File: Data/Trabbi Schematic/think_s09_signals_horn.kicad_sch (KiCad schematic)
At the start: 15 parts, among them J1 Power Outlet (D60), K1 Flasher Relay R3, SW1 Horn Contact (steering wheel), SW2 Turn Signal / Hazard Switch (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, SW3 Driver Door Switch (C30), SW4 Passenger Door Switch (C31), SW5 Tailgate Switch (B10)

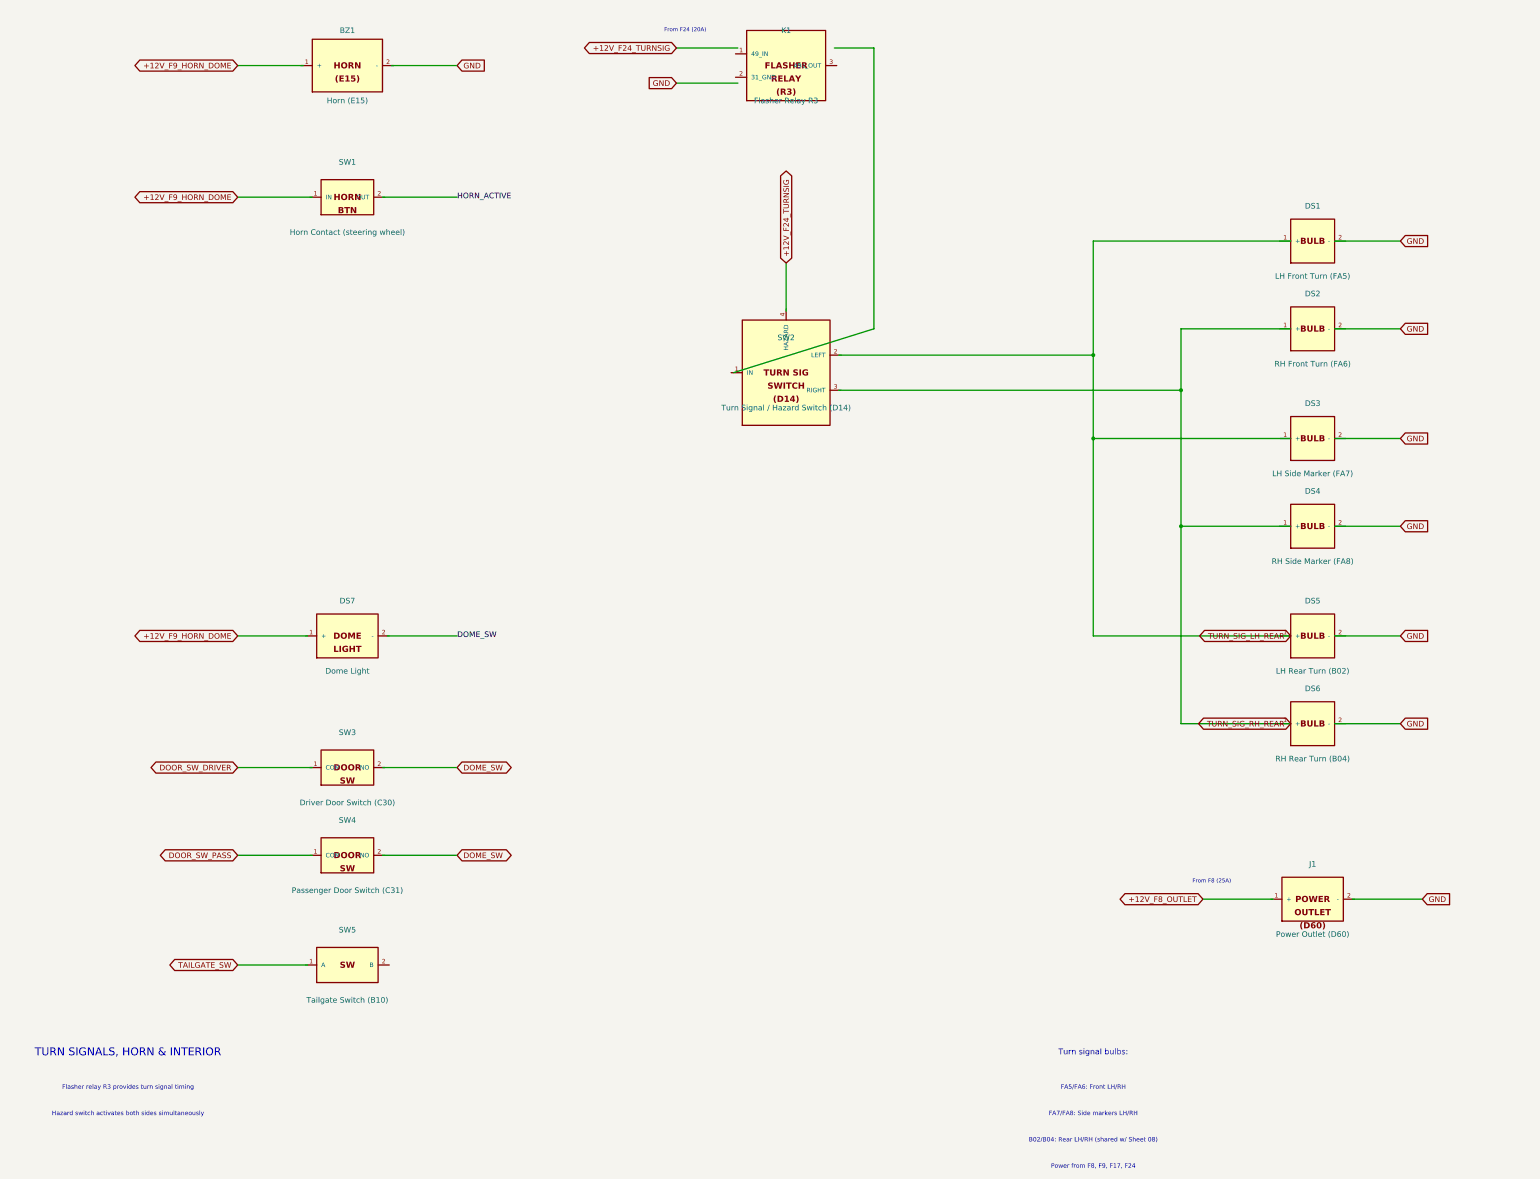
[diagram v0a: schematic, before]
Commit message: Fix wire-to-pin connections: use exact calculated pin positions
Refactored gen_think_complete.py to compute exact pin schematic
coordinates instead of using approximate manual offsets. Added p()
method to Sheet class that transforms symbol-local pin positions to
schematic coordinates. All 232 wire calls across 13 sub-sheet
generators now use p() for pin endpoints, fixing misaligned
connections (previously off by 0.54-10+ units).

Co-Authored-By: Claude Opus 4.6 <noreply@anthropic.com>
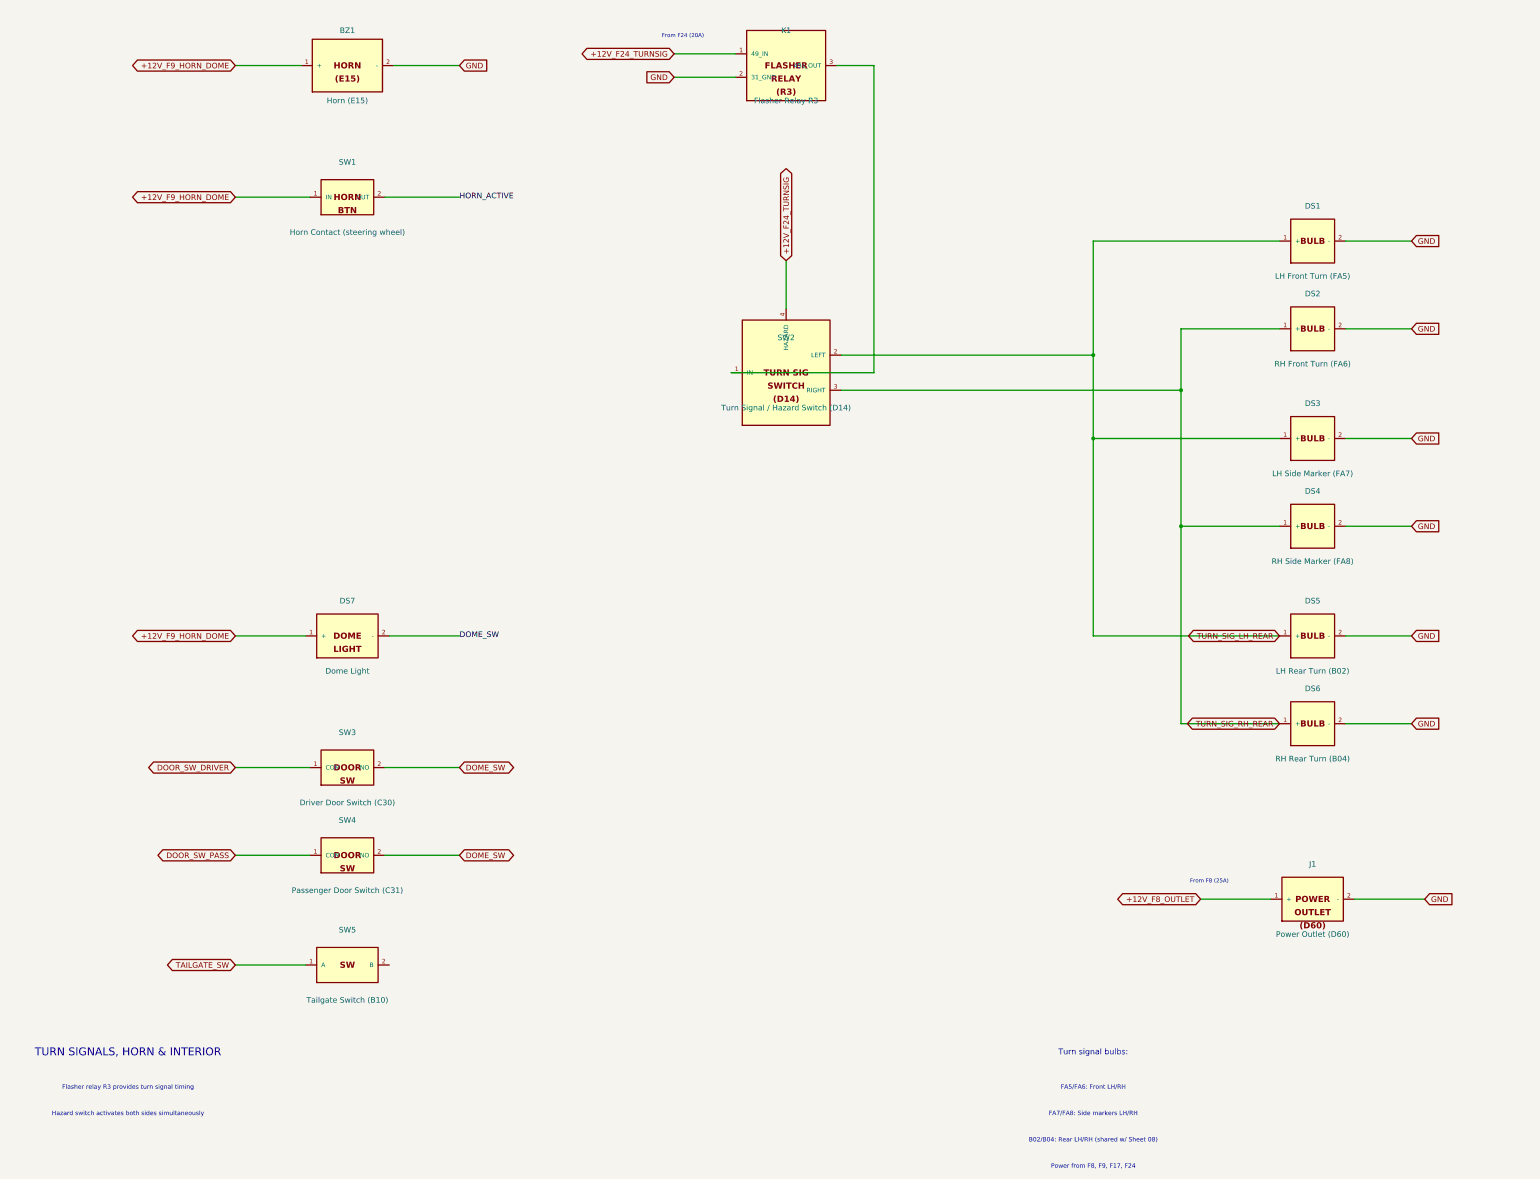
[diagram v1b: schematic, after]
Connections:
- net +12V_F24_TURNSIG: now also K1.1 (49_IN), SW2.4 (HAZARD)
- net +12V_F8_OUTLET: now also J1.1 (+)
- net +12V_F9_HORN_DOME: now also BZ1.1 (+), DS7.1 (+), SW1.1 (IN)
- net DOME_SW: now also DS7.2 (-), SW3.2 (NO), SW4.2 (NO)
- net DOOR_SW_DRIVER: now also SW3.1 (COM)
- net DOOR_SW_PASS: now also SW4.1 (COM)
- net GND: now also BZ1.2 (-), DS1.2 (-), DS2.2 (-), DS3.2 (-), DS4.2 (-), DS5.2 (-), DS6.2 (-), J1.2 (-), K1.2 (31_GND)
- net HORN_ACTIVE: now also SW1.2 (OUT)
- net TAILGATE_SW: now also SW5.1 (A)
- net TURN_SIG_LH_REAR: now also DS1.1 (+), DS3.1 (+), DS5.1 (+), SW2.2 (LEFT)
- net TURN_SIG_RH_REAR: now also DS2.1 (+), DS4.1 (+), DS6.1 (+), SW2.3 (RIGHT)
- net at SW2.1 (IN): now also K1.3 (49a_OUT)

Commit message: Enforce orthogonal routing and 1.27mm grid alignment
- Add _g() grid snap function to Sheet class (rounds all coordinates to nearest 1.27mm)
- Add wire_l() method for L-shaped orthogonal routing (horizontal+vertical segments)
- Apply grid snapping in p(), place(), wire(), label(), glabel(), junction(), no_connect(), defsym()
- Replace all 19 diagonal wire calls with wire_l() across S02, S06, S07, S08, S10, S12, S13
- All wire segments now strictly horizontal or vertical, no diagonals
- All coordinates verified on 1.27mm (50mil) KiCad standard grid

Co-Authored-By: Claude Opus 4.6 <noreply@anthropic.com>
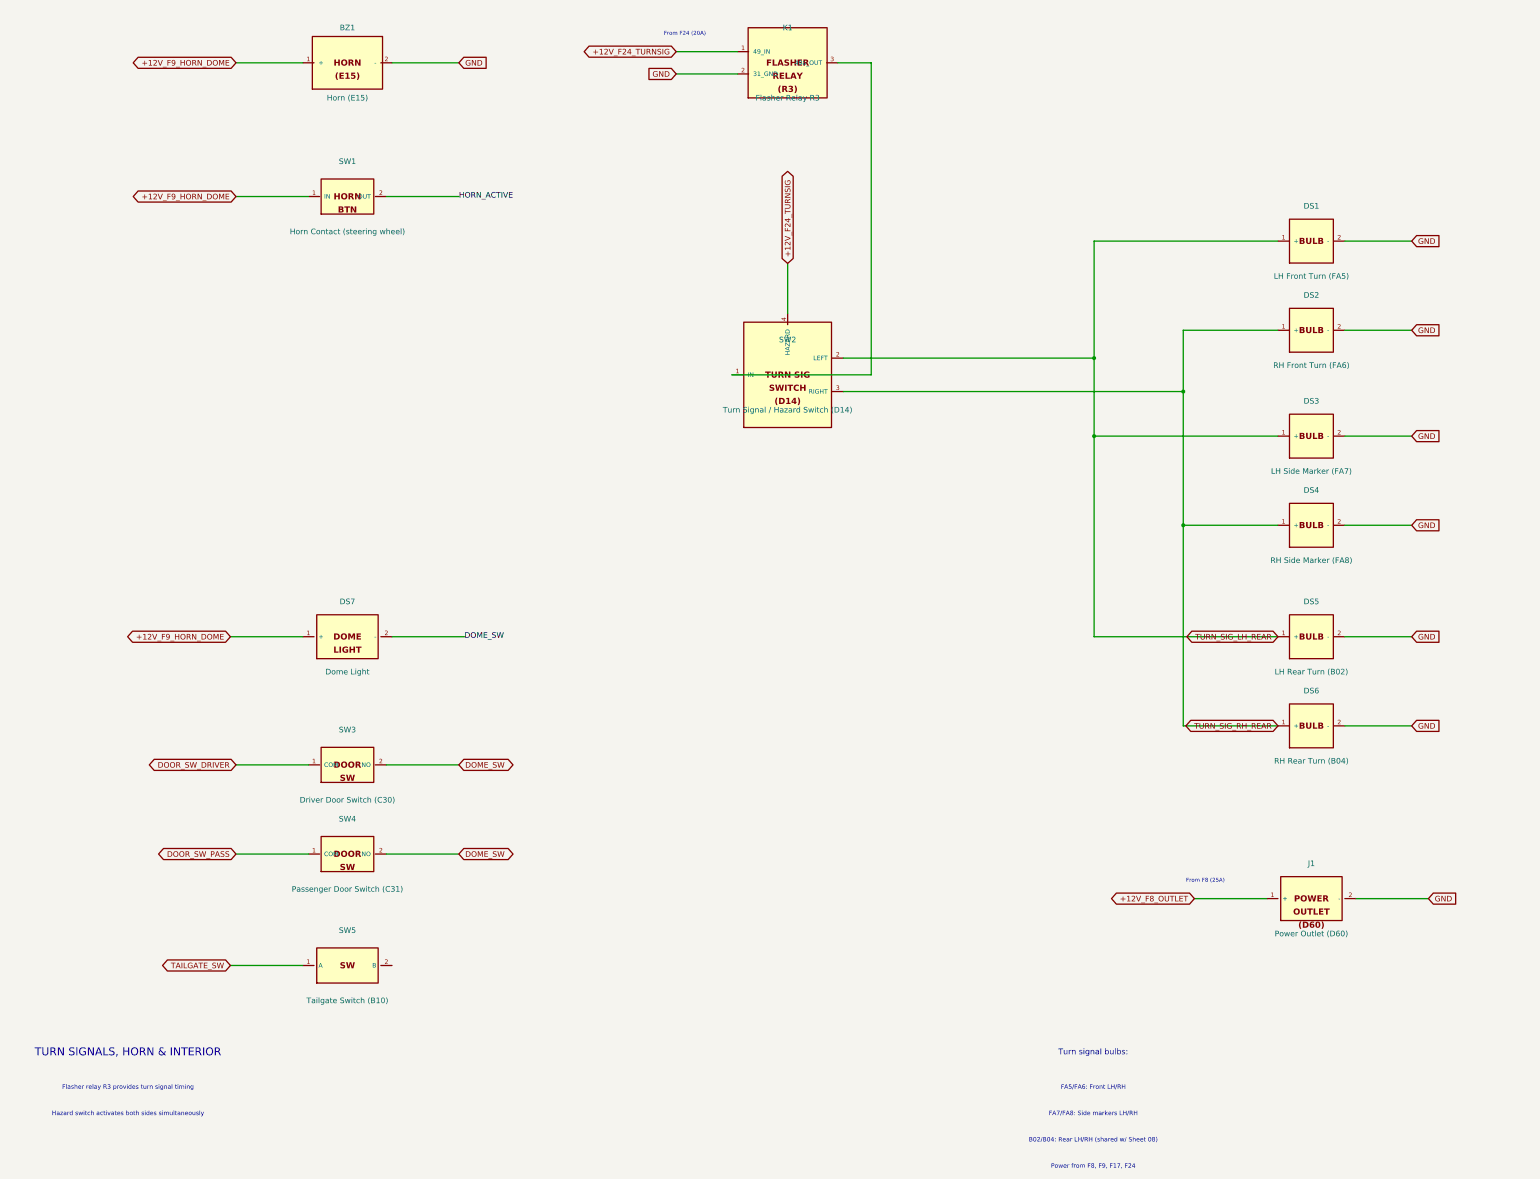
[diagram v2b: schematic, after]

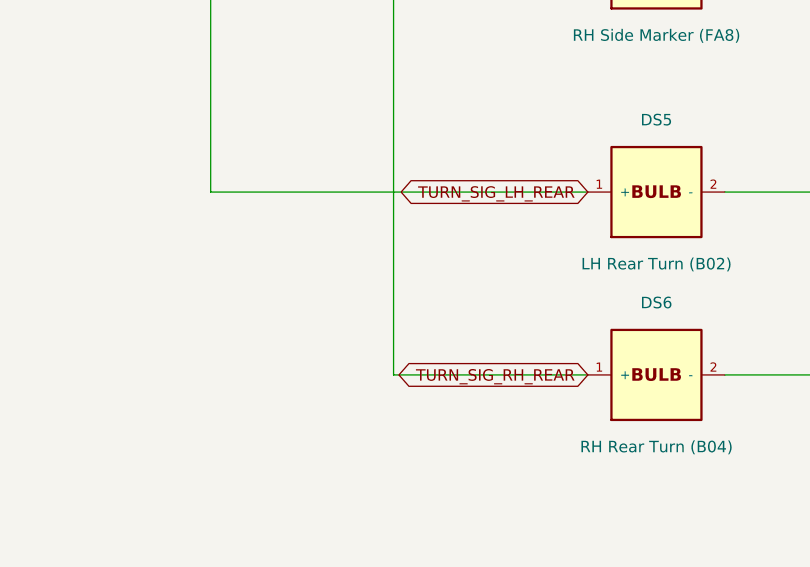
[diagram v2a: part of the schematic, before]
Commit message: Add relay coil/switch graphics, fix label positioning
- Draw coil (inductor arcs) and switch contacts (circles + arm)
  inside RELAY_SPST and RELAY_SPDT symbol bodies
- Add body_gfx parameter to defsym() for custom symbol graphics
- Helper functions: _gfx_polyline, _gfx_arc, _gfx_circle, _relay_gfx
- Fix label offsets: increase from 3-5mm to 10-12mm to avoid
  overlapping pin names (S01 ignition, S02 HV, S05 DCDC, S07 lights)
- Fix S09 turn signal rear labels: add wire stubs (were at 0 offset)
- All 14 schematics regenerated, parentheses balanced, grid OK

Co-Authored-By: Claude Opus 4.6 <noreply@anthropic.com>
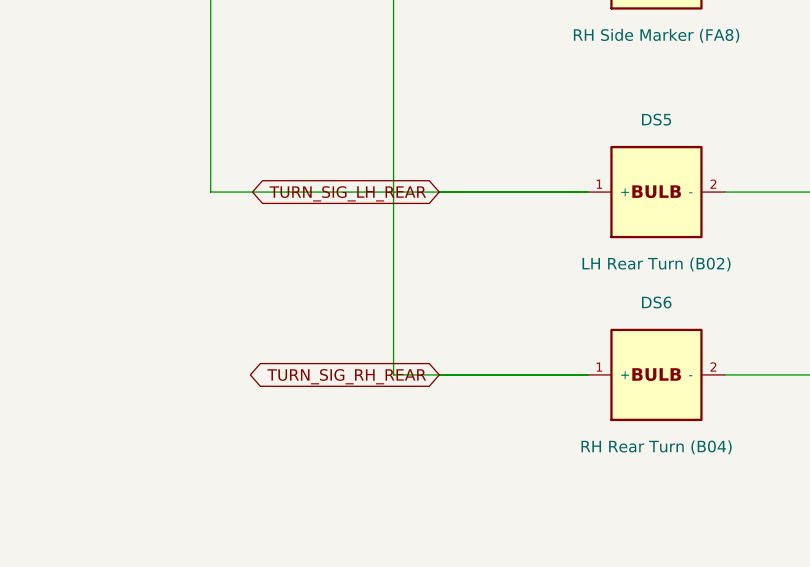
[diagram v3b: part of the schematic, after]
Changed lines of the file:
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@@
     )
   )
-  (global_label "TURN_SIG_LH_REAR" (shape bidirectional) (at 292.100 170.180 180)
+  (wire (pts (xy 292.100 170.180) (xy 275.590 170.180))
+    (stroke (width 0) (type default))
+  )
+  (global_label "TURN_SIG_LH_REAR" (shape bidirectional) (at 275.590 170.180 180)
     (effects (font (size 1.27 1.27)))
-    (property "Intersheetrefs" "${INTERSHEET_REFS}" (at 292.100 170.180 0)
+    (property "Intersheetrefs" "${INTERSHEET_REFS}" (at 275.590 170.180 0)
       (effects (font (size 1.27 1.27)) hide)
     )
   )
-  (global_label "TURN_SIG_RH_REAR" (shape bidirectional) (at 292.100 190.500 180)
+  (wire (pts (xy 292.100 190.500) (xy 275.590 190.500))
+    (stroke (width 0) (type default))
+  )
+  (global_label "TURN_SIG_RH_REAR" (shape bidirectional) (at 275.590 190.500 180)
     (effects (font (size 1.27 1.27)))
-    (property "Intersheetrefs" "${INTERSHEET_REFS}" (at 292.100 190.500 0)
+    (property "Intersheetrefs" "${INTERSHEET_REFS}" (at 275.590 190.500 0)
       (effects (font (size 1.27 1.27)) hide)
     )
